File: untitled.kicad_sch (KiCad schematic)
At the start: 25 parts, among them J4 Conn_01x15_Pin, J5 Conn_01x15_Pin, SW3 SW_SPDT, U5 STM32F103CBT6, Y1 16MHZ

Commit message: issues solved!!
Streamlined the design by resolving CP2102N and ESP32 TX/RX pin issues. All necessary footprints were assigned, favoring 0805 SMD components for a compact board layout
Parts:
- C10, C11, C12, C13, C14, C15, C16, C17, C18, C19: footprint (none) -> Capacitor_SMD:C_0805_2012Metric_Pad1.18x1.45mm_HandSolder
- D10, D11, D8, D9: footprint (none) -> LED_SMD:LED_0805_2012Metric_Pad1.15x1.40mm_HandSolder
- FB1: footprint (none) -> Inductor_SMD:L_0805_2012Metric_Pad1.05x1.20mm_HandSolder
- J4, J5: footprint (none) -> Connector_PinHeader_2.54mm:PinHeader_1x15_P2.54mm_Vertical
- R13, R14, R18, R19, R20: footprint (none) -> Resistor_SMD:R_0805_2012Metric_Pad1.20x1.40mm_HandSolder
- SW3: footprint (none) -> Button_Switch_THT:SW_Push_1P2T_Vertical_E-Switch_800UDP8P1A1M6
- Y1: footprint (none) -> Crystal:Crystal_SMD_2016-4Pin_2.0x1.6mm
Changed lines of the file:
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@@
 	(title_block
 		(title "STM32 ")
-		(date "2025-07-03")
+		(date "2025-07-25")
 		(rev "1")
 		(company "OMKAR NANAJKAR")
@@
 			)
 		)
-		(property "Footprint" ""
+		(property "Footprint" "Connector_PinHeader_2.54mm:PinHeader_1x15_P2.54mm_Vertical"
 			(at 196.85 144.78 0)
 			(effects
@@
 			)
 		)
-		(property "Footprint" ""
+		(property "Footprint" "Capacitor_SMD:C_0805_2012Metric_Pad1.18x1.45mm_HandSolder"
 			(at 155.9052 74.93 0)
 			(effects
@@
 			)
 		)
-		(property "Footprint" ""
+		(property "Footprint" "LED_SMD:LED_0805_2012Metric_Pad1.15x1.40mm_HandSolder"
 			(at 224.79 81.28 0)
 			(effects
@@
 			)
 		)
-		(property "Footprint" ""
+		(property "Footprint" "Capacitor_SMD:C_0805_2012Metric_Pad1.18x1.45mm_HandSolder"
 			(at 32.7152 92.71 0)
 			(effects
@@
 			)
 		)
-		(property "Footprint" ""
+		(property "Footprint" "Inductor_SMD:L_0805_2012Metric_Pad1.05x1.20mm_HandSolder"
 			(at 146.05 69.088 90)
 			(effects
@@
 			)
 		)
-		(property "Footprint" ""
+		(property "Footprint" "Capacitor_SMD:C_0805_2012Metric_Pad1.18x1.45mm_HandSolder"
 			(at 60.6552 74.93 0)
 			(effects
@@
 			)
 		)
-		(property "Footprint" ""
+		(property "Footprint" "Connector_PinHeader_2.54mm:PinHeader_1x15_P2.54mm_Vertical"
 			(at 246.38 144.78 0)
 			(effects
@@
 			)
 		)
-		(property "Footprint" ""
+		(property "Footprint" "Resistor_SMD:R_0805_2012Metric_Pad1.20x1.40mm_HandSolder"
 			(at 211.582 73.66 90)
 			(effects
@@
 			)
 		)
-		(property "Footprint" ""
+		(property "Footprint" "LED_SMD:LED_0805_2012Metric_Pad1.15x1.40mm_HandSolder"
 			(at 226.06 106.68 0)
 			(effects
@@
 			)
 		)
-		(property "Footprint" ""
+		(property "Footprint" "Capacitor_SMD:C_0805_2012Metric_Pad1.18x1.45mm_HandSolder"
 			(at 117.8052 74.93 0)
 			(effects
@@
 			)
 		)
-		(property "Footprint" ""
+		(property "Footprint" "Capacitor_SMD:C_0805_2012Metric_Pad1.18x1.45mm_HandSolder"
 			(at 47.9552 74.93 0)
 			(effects
@@
 			)
 		)
-		(property "Footprint" ""
+		(property "Footprint" "Resistor_SMD:R_0805_2012Metric_Pad1.20x1.40mm_HandSolder"
 			(at 211.582 31.75 90)
 			(effects
@@
 			)
 		)
-		(property "Footprint" ""
+		(property "Footprint" "Capacitor_SMD:C_0805_2012Metric_Pad1.18x1.45mm_HandSolder"
 			(at 133.0452 74.93 0)
 			(effects
@@
 			)
 		)
-		(property "Footprint" ""
+		(property "Footprint" "Capacitor_SMD:C_0805_2012Metric_Pad1.18x1.45mm_HandSolder"
 			(at 68.2752 114.3 0)
 			(effects
@@
 			)
 		)
-		(property "Footprint" ""
+		(property "Footprint" "Resistor_SMD:R_0805_2012Metric_Pad1.20x1.40mm_HandSolder"
 			(at 64.77 91.948 90)
 			(effects
@@
 			)
 		)
-		(property "Footprint" ""
+		(property "Footprint" "LED_SMD:LED_0805_2012Metric_Pad1.15x1.40mm_HandSolder"
 			(at 224.79 63.5 0)
 			(effects
@@
 			)
 		)
-		(property "Footprint" ""
+		(property "Footprint" "Crystal:Crystal_SMD_2016-4Pin_2.0x1.6mm"
 			(at 52.07 104.14 0)
 			(effects
@@
 			)
 		)
-		(property "Footprint" ""
+		(property "Footprint" "Resistor_SMD:R_0805_2012Metric_Pad1.20x1.40mm_HandSolder"
 			(at 211.582 57.15 90)
 			(effects
@@
 			)
 		)
-		(property "Footprint" ""
+		(property "Footprint" "Capacitor_SMD:C_0805_2012Metric_Pad1.18x1.45mm_HandSolder"
 			(at 40.3352 114.3 0)
 			(effects
@@
 			)
 		)
-		(property "Footprint" ""
+		(property "Footprint" "LED_SMD:LED_0805_2012Metric_Pad1.15x1.40mm_HandSolder"
 			(at 224.79 38.1 0)
 			(effects
@@
 			)
 		)
-		(property "Footprint" ""
+		(property "Footprint" "Resistor_SMD:R_0805_2012Metric_Pad1.20x1.40mm_HandSolder"
 			(at 211.582 99.06 90)
 			(effects
@@
 			)
 		)
-		(property "Footprint" ""
+		(property "Footprint" "Capacitor_SMD:C_0805_2012Metric_Pad1.18x1.45mm_HandSolder"
 			(at 73.3552 74.93 0)
 			(effects
@@
 			)
 		)
-		(property "Footprint" ""
+		(property "Footprint" "Capacitor_SMD:C_0805_2012Metric_Pad1.18x1.45mm_HandSolder"
 			(at 35.2552 74.93 0)
 			(effects
@@
 			)
 		)
-		(property "Footprint" ""
+		(property "Footprint" "Button_Switch_THT:SW_Push_1P2T_Vertical_E-Switch_800UDP8P1A1M6"
 			(at 55.88 90.17 0)
 			(effects

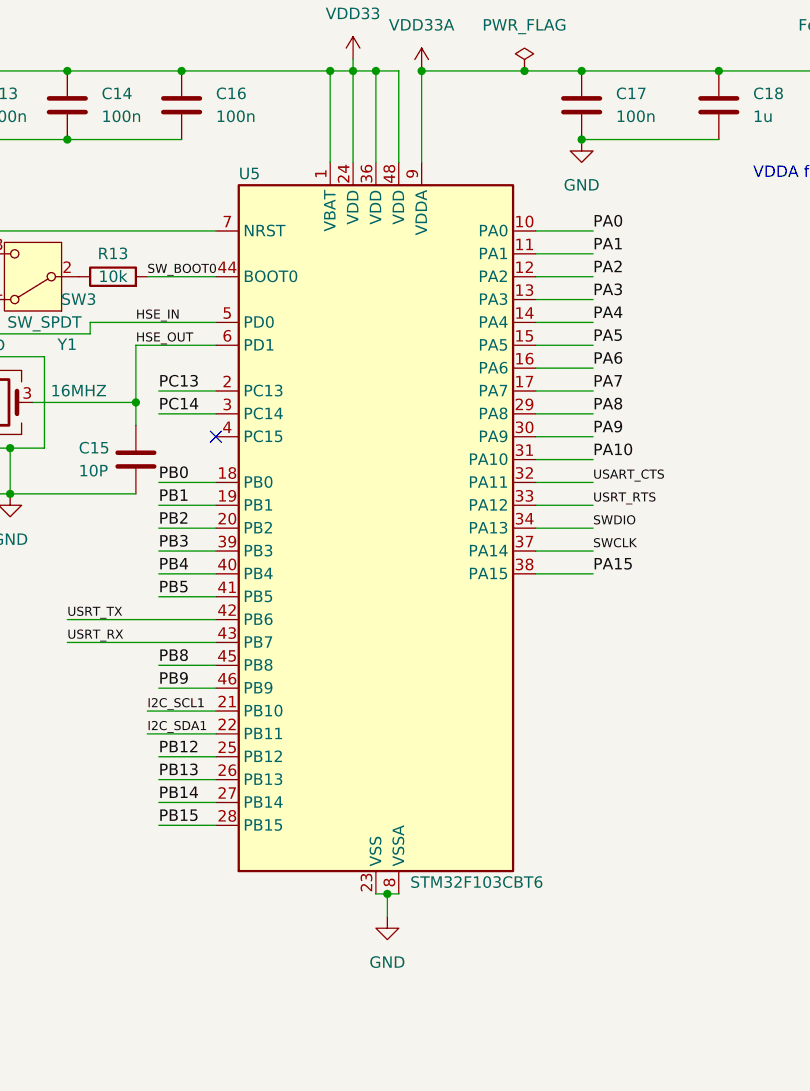
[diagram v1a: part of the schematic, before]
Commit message: STM32F103C8t6 is changed to STM32F103C6tx
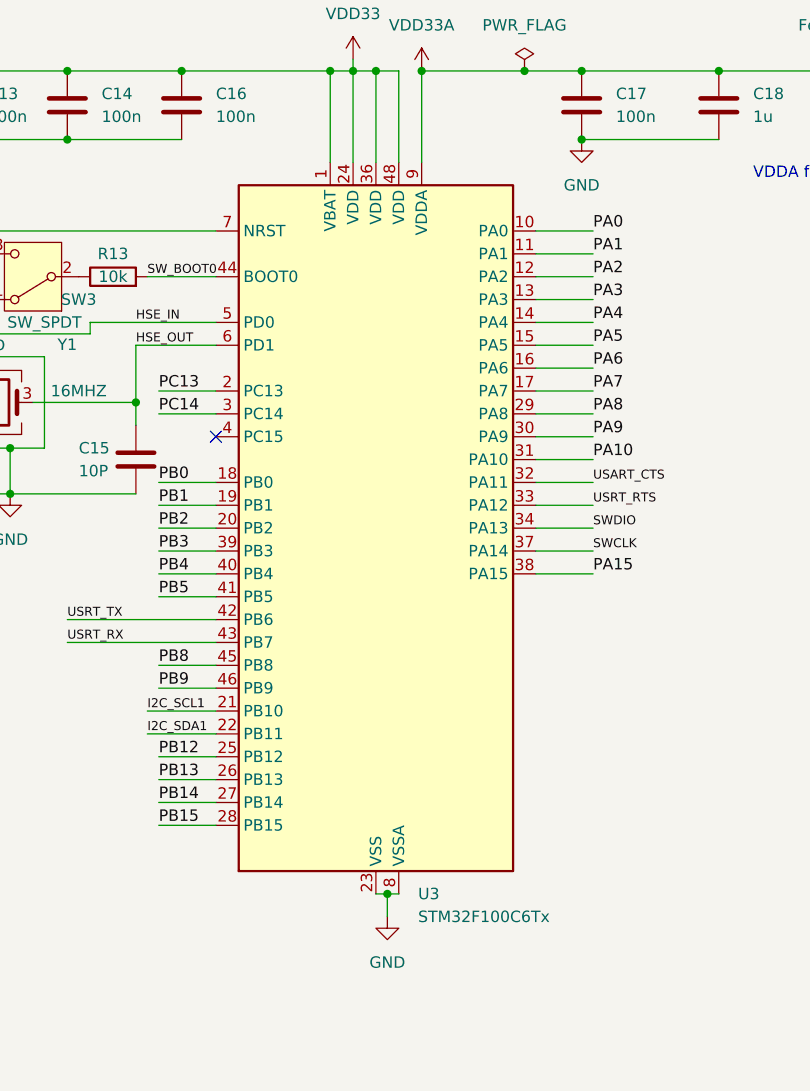
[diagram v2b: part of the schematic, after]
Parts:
- removed U5: STM32F103CBT6, Package_QFP:LQFP-48_7x7mm_P0.5mm, symbol MCU_ST_STM32F1:STM32F103CBTx
- added U3: STM32F100C6Tx, Package_QFP:LQFP-48_7x7mm_P0.5mm, symbol MCU_ST_STM32F1:STM32F100C6Tx
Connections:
- net CTS: now also U3.33 (PA12)
- net GND: now also U3.23 (VSS), U3.35 (VSS), U3.47 (VSS), U3.8 (VSSA)
- net HSE_IN: now also U3.5 (PD0)
- net HSE_OUT: now also U3.6 (PD1)
- net I2C_SCL1: now also U3.21 (PB10)
- net I2C_SDA1: now also U3.22 (PB11)
- net NRST: now also U3.7 (NRST)
- net PA0: now also U3.10 (PA0)
- net PA1: now also U3.11 (PA1)
- net PA10: now also U3.31 (PA10)
- net PA15: now also U3.38 (PA15)
- net PA2: now also U3.12 (PA2)
- net PA3: now also U3.13 (PA3)
- net PA4: now also U3.14 (PA4)
- net PA5: now also U3.15 (PA5)
- net PA6: now also U3.16 (PA6)
- net PA7: now also U3.17 (PA7)
- net PA8: now also U3.29 (PA8)
- net PA9: now also U3.30 (PA9)
- net PB0: now also U3.18 (PB0)
- net PB1: now also U3.19 (PB1)
- net PB12: now also U3.25 (PB12)
- net PB13: now also U3.26 (PB13)
- net PB14: now also U3.27 (PB14)
- net PB15: now also U3.28 (PB15)
- net PB2: now also U3.20 (PB2)
- net PB3: now also U3.39 (PB3)
- net PB4: now also U3.40 (PB4)
- net PB5: now also U3.41 (PB5)
- net PB8: now also U3.45 (PB8)
- net PB9: now also U3.46 (PB9)
- net PC13: now also U3.2 (PC13)
- net PC14: now also U3.3 (PC14)
- net RTS: now also U3.32 (PA11)
- net RXD0: now also U3.42 (PB6)
- net SWCLK: now also U3.37 (PA14)
- net SWDIO: now also U3.34 (PA13)
- net SW_BOOT0: now also U3.44 (BOOT0)
- net TXD0: now also U3.43 (PB7)
- net VDD33: now also U3.1 (VBAT), U3.24 (VDD), U3.36 (VDD), U3.48 (VDD)
- net VDD33A: now also U3.9 (VDDA)
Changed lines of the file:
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@@
-	)
-	(symbol
-		(lib_id "MCU_ST_STM32F1:STM32F103CBTx")
-		(at 93.98 118.11 0)
-		(unit 1)
-		(exclude_from_sim no)
-		(in_bom yes)
-		(on_board yes)
-		(dnp no)
-		(property "Reference" "U5"
-			(at 78.74 78.74 0)
-			(effects
-				(font
-					(size 1.27 1.27)
-				)
-				(justify left)
-			)
-		)
-		(property "Value" "STM32F103CBT6"
-			(at 97.79 157.48 0)
-			(effects
-				(font
-					(size 1.27 1.27)
-				)
-				(justify left)
-			)
-		)
-		(property "Footprint" "Package_QFP:LQFP-48_7x7mm_P0.5mm"
-			(at 78.74 156.21 0)
-			(effects
-				(font
-					(size 1.27 1.27)
-				)
-				(justify right)
-				(hide yes)
-			)
-		)
-		(property "Datasheet" "https://www.st.com/resource/en/datasheet/stm32f103cb.pdf"
-			(at 93.98 118.11 0)
-			(effects
-				(font
-					(size 1.27 1.27)
-				)
-				(hide yes)
-			)
-		)
-		(property "Description" "STMicroelectronics Arm Cortex-M3 MCU, 128KB flash, 20KB RAM, 72 MHz, 2.0-3.6V, 37 GPIO, LQFP48"
-			(at 93.98 118.11 0)
-			(effects
-				(font
-					(size 1.27 1.27)
-				)
-				(hide yes)
-			)
-		)
-		(pin "44"
-		)
-		(pin "7"
-		)
-		(pin "4"
-		)
-		(pin "20"
-		)
-		(pin "41"
-		)
-		(pin "42"
-		)
-		(pin "5"
-		)
-		(pin "2"
-		)
-		(pin "6"
-		)
-		(pin "3"
-		)
-		(pin "18"
-		)
-		(pin "19"
-		)
-		(pin "39"
-		)
-		(pin "40"
-		)
-		(pin "12"
-		)
-		(pin "15"
-		)
-		(pin "47"
-		)
-		(pin "28"
-		)
-		(pin "25"
-		)
-		(pin "35"
-		)
-		(pin "22"
-		)
-		(pin "36"
-		)
-		(pin "21"
-		)
-		(pin "48"
-		)
-		(pin "45"
-		)
-		(pin "26"
-		)
-		(pin "8"
-		)
-		(pin "43"
-		)
-		(pin "1"
-		)
-		(pin "27"
-		)
-		(pin "9"
-		)
-		(pin "10"
-		)
-		(pin "14"
-		)
-		(pin "46"
-		)
-		(pin "24"
-		)
-		(pin "23"
-		)
-		(pin "11"
-		)
-		(pin "13"
-		)
-		(pin "29"
-		)
-		(pin "32"
-		)
-		(pin "33"
-		)
-		(pin "31"
-		)
-		(pin "17"
-		)
-		(pin "37"
-		)
-		(pin "34"
-		)
-		(pin "30"
-		)
-		(pin "38"
-		)
-		(pin "16"
-		)
-		(instances
-			(project "4 SRA"
-				(path "/88b20362-4bc6-47a6-a0e3-d53b76e5c5a4/4d43ffad-1280-4d9e-8621-d545659bd031"
-					(reference "U5")
-					(unit 1)
-				)
-			)
-		)
 	)
 	(symbol
@@
 					(unit 1)
 				)
+			)
+		)
+	)
+	(symbol
+		(lib_id "MCU_ST_STM32F1:STM32F100C6Tx")
+		(at 93.98 118.11 0)
+		(unit 1)
+		(exclude_from_sim no)
+		(in_bom yes)
+		(on_board yes)
+		(dnp no)
+		(fields_autoplaced yes)
+		(property "Reference" "U3"
+			(at 98.6633 158.75 0)
+			(effects
+				(font
+					(size 1.27 1.27)
+				)
+				(justify left)
+			)
+		)
+		(property "Value" "STM32F100C6Tx"
+			(at 98.6633 161.29 0)
+			(effects
+				(font
+					(size 1.27 1.27)
+				)
+				(justify left)
+			)
+		)
+		(property "Footprint" "Package_QFP:LQFP-48_7x7mm_P0.5mm"
+			(at 78.74 156.21 0)
+			(effects
+				(font
+					(size 1.27 1.27)
+				)
+				(justify right)
+				(hide yes)
+			)
+		)
+		(property "Datasheet" "https://www.st.com/resource/en/datasheet/stm32f100c6.pdf"
+			(at 93.98 118.11 0)
+			(effects
+				(font
+					(size 1.27 1.27)
+				)
+				(hide yes)
+			)
+		)
+		(property "Description" "STMicroelectronics Arm Cortex-M3 MCU, 32KB flash, 4KB RAM, 24 MHz, 2.0-3.6V, 37 GPIO, LQFP48"
+			(at 93.98 118.11 0)
+			(effects
+				(font
+					(size 1.27 1.27)
+				)
+				(hide yes)
+			)
+		)
+		(pin "3"
+		)
+		(pin "43"
+		)
+		(pin "46"
+		)
+		(pin "20"
+		)
+		(pin "25"
+		)
+		(pin "18"
+		)
+		(pin "28"
+		)
+		(pin "7"
+		)
+		(pin "2"
+		)
+		(pin "6"
+		)
+		(pin "4"
+		)
+		(pin "19"
+		)
+		(pin "44"
+		)
+		(pin "40"
+		)
+		(pin "5"
+		)
+		(pin "39"
+		)
+		(pin "41"
+		)
+		(pin "42"
+		)
+		(pin "45"
+		)
+		(pin "21"
+		)
+		(pin "22"
+		)
+		(pin "27"
+		)
+		(pin "26"
+		)
+		(pin "15"
+		)
+		(pin "36"
+		)
+		(pin "48"
+		)
+		(pin "13"
+		)
+		(pin "31"
+		)
+		(pin "24"
+		)
+		(pin "34"
+		)
+		(pin "9"
+		)
+		(pin "37"
+		)
+		(pin "38"
+		)
+		(pin "12"
+		)
+		(pin "32"
+		)
+		(pin "29"
+		)
+		(pin "10"
+		)
+		(pin "17"
+		)
+		(pin "1"
+		)
+		(pin "11"
+		)
+		(pin "16"
+		)
+		(pin "30"
+		)
+		(pin "35"
+		)
+		(pin "47"
+		)
+		(pin "14"
+		)
+		(pin "23"
+		)
+		(pin "8"
+		)
+		(pin "33"
+		)
+		(instances
+			(project ""
+				(path "/88b20362-4bc6-47a6-a0e3-d53b76e5c5a4/4d43ffad-1280-4d9e-8621-d545659bd031"
+					(reference "U3")
+					(unit 1)
+				)

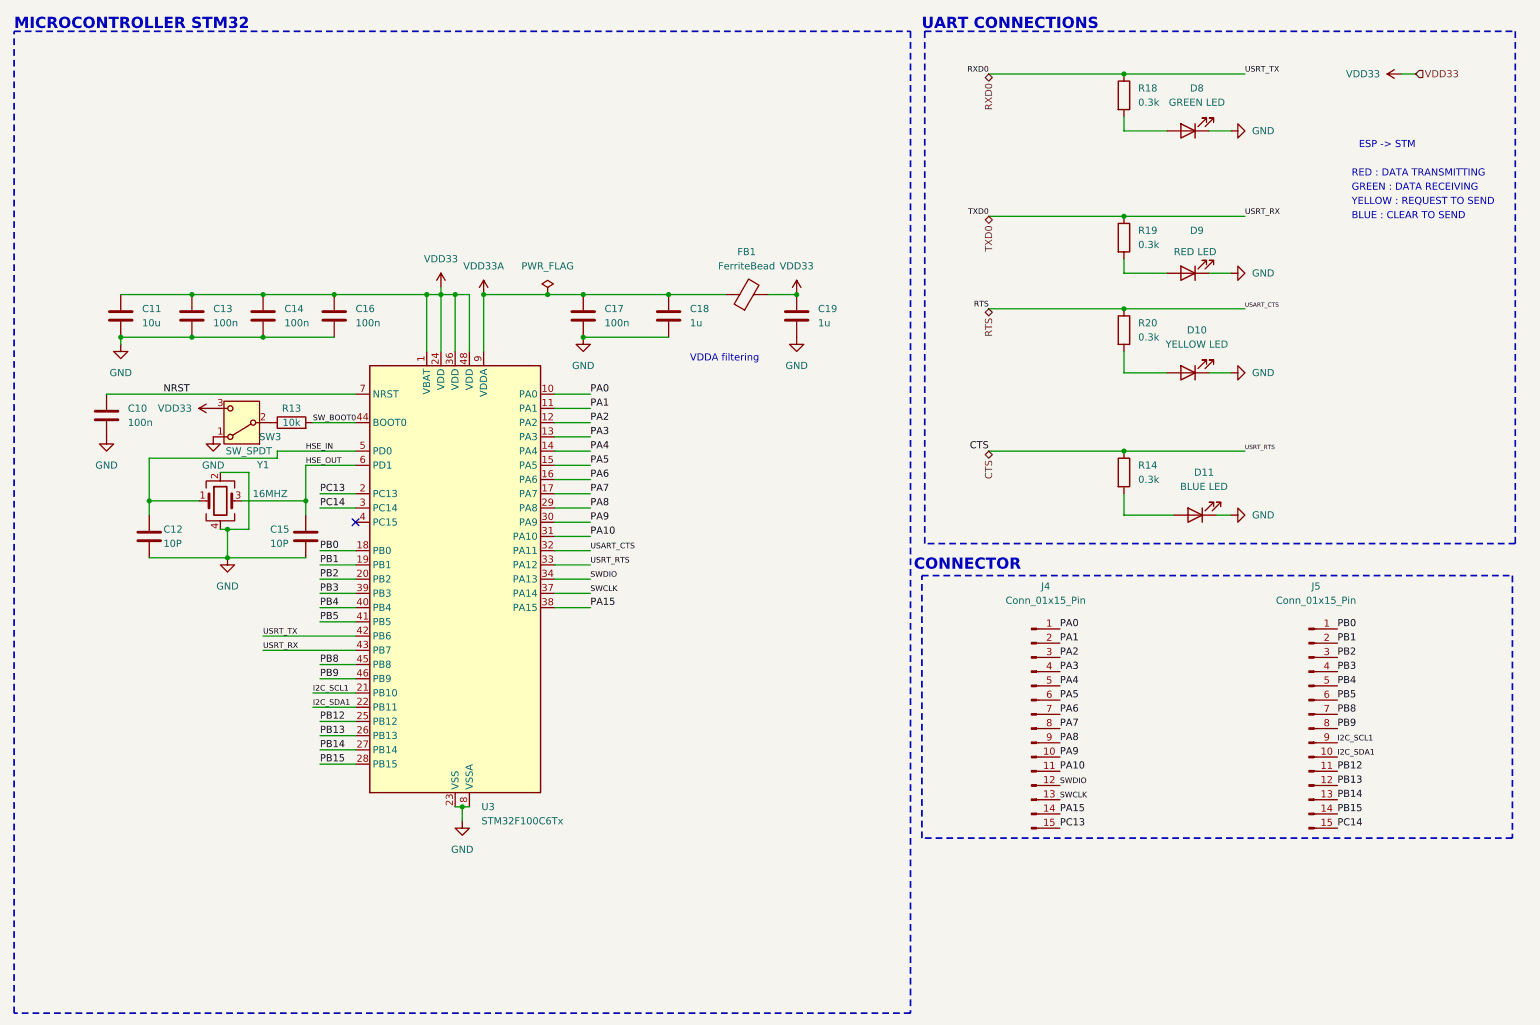
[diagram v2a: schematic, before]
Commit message: Battery System Integration Complete
Added comprehensive battery functionality to the development board, including integrated battery protection circuitry and USB-C charging capability. All schematics have been updated to reflect the new power management topology and charging infrastructure
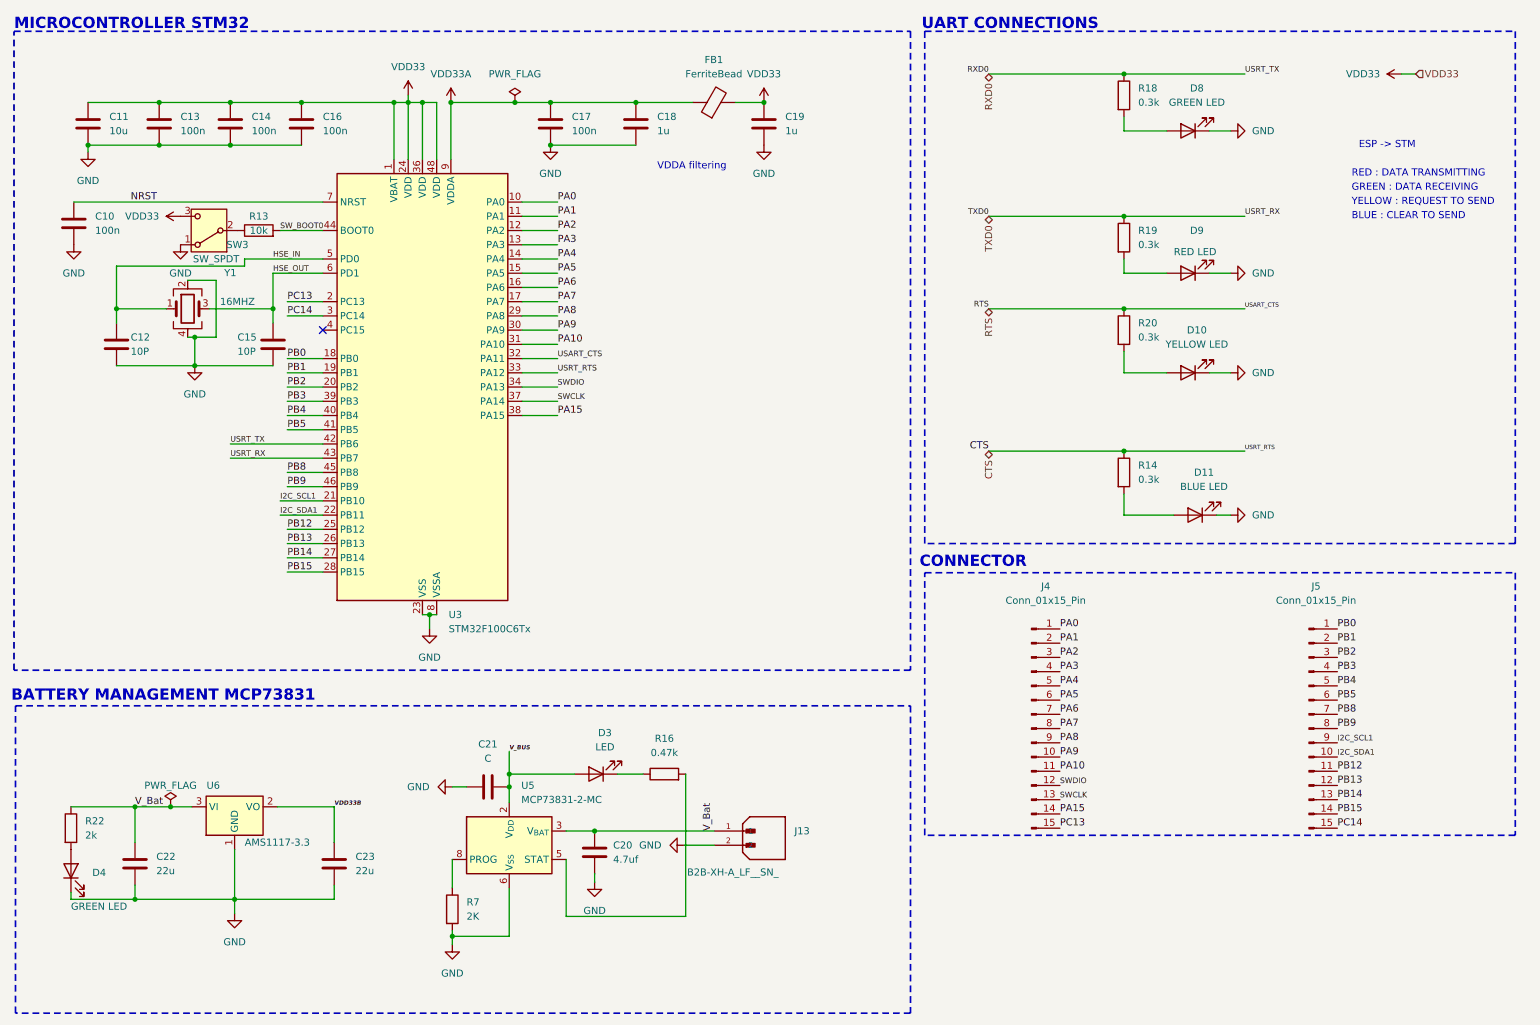
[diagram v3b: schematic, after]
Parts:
- added C20: 4.7uf, symbol Device:C
- added C21: C, symbol Device:C
- added C22, C23: 22u, Capacitor_SMD:C_0805_2012Metric_Pad1.18x1.45mm_HandSolder, symbol Device:C
- added D3: LED, symbol Device:LED
- added D4: GREEN LED, LED_SMD:LED_0805_2012Metric_Pad1.15x1.40mm_HandSolder, symbol Device:LED
- added J13: B2B-XH-A_LF__SN_, JST Connector:2 Pin JST Connector, symbol Power JST:B2B-XH-A_LF__SN_
- added R16: 0.47k, symbol Device:R
- added R22: 2k, Resistor_SMD:R_0805_2012Metric_Pad1.20x1.40mm_HandSolder, symbol Device:R
- added R7: 2K, symbol Device:R
- added U5: MCP73831-2-MC, Package_DFN_QFN:DFN-8-1EP_3x2mm_P0.5mm_EP1.7x1.4mm, symbol Battery_Management:MCP73831-2-MC
- added U6: AMS1117-3.3, Package_TO_SOT_SMD:SOT-223-3_TabPin2, symbol Regulator_Linear:AMS1117-3.3
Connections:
- net GND: now also C20.2, C21.1, C22.2, C23.2, D4.1 (K), J13.2, R7.2, U5.6 (V_{SS}), U6.1 (GND)
- new net: R7.1, U5.8 (PROG)
- new net: D4.2 (A), R22.2
- new net: R16.2, U5.5 (STAT)
- new net: D3.1 (K), R16.1
- new net VDD33B: C23.1, U6.2 (VO)
- new net V_BUS: C21.2, D3.2 (A), U5.1 (V_{DD}), U5.2 (V_{DD})
- new net V_Bat: C20.1, C22.1, J13.1, R22.1, U5.3 (V_{BAT}), U5.4 (V_{BAT}), U6.3 (VI)
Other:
- note added: "BATTERY MANAGEMENT MCP73831"
- moved on the sheet: C10, C11, C12, C13, C14, C15, C16, C17, C18, C19, FB1, R13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
